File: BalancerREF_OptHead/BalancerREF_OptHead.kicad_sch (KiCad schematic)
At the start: 24 parts, among them J5 TO MAIN BOARD, Q1 AO3400A, U4 TS3021IYLT, U8 TLV9062IDR

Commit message: fix: flip PD1 - the optical comparator could never trip
Confirmed against the netlist, not the description. PD1 was wired cathode to
+3V3 and anode to the transimpedance summing node. The reverse bias is correct
that way, 1.65 V cathode-positive, which is presumably why it survived this long.
The signal direction is not.

Photocurrent leaves the ANODE of a reverse-biased photodiode, so with the anode
on the summing node it was injected into the node rather than pulled out:

  PD1 anode on the node  -> current INTO the summing node
  U8A, U8.2 = IN-        -> inverting TIA, TIA_OUT FALLS
  U8B, gain -120k/10k    -> inverting, OPT_AMP RISES from 1.65 V
  U4, U8.4 = IN-         -> against CMP_THRESHOLD on IN+

CMP_THRESHOLD is 3.3 * 10k/(22k+10k) = 1.016 V with the output low, 1.064 V with
it high - R28's 470k gives 48 mV of hysteresis in the correct direction.
OPT_AMP idles at 1.65 V, AC-coupled to the 1.65 V reference, so it sits 634 mV
ABOVE the threshold and light drove it further away. IN- stayed above IN+ at any
illumination and the output never left its low state. With the Rev F NAND gating
that is total: U9 never falls, U10 never triggers, TR-VERT had no tach at all.

Flipping the diode fixes the chain without touching anything else. Cathode to
PD_TIA_IN, anode to GND: same 1.65 V reverse bias, photocurrent now pulled out of
the node, TIA_OUT rises, OPT_AMP falls through 1.016 V, comparator trips. It
takes about 5.3 uA of photocurrent - 634 mV / 12 / 10k.

Side effect worth having, since Rev F moved Q1 nearer PD1 when it tightened the
emitter loop: the emitter turn-off edge lands inside the synchronous gate window
and cannot be rejected, and after the flip its coupling into the summing node
pushes TIA_OUT the same way darkness does, away from the trip point.

Why none of the existing checks found it. verify_head.py compares the exported
netlist against exact net membership and passed throughout - netlist matched
spec, board matched netlist, ERC clean - because 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
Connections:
- net +3V3: no longer PD1.1 (K)
- net GND: now also PD1.2 (A)
- net PD_TIA_IN: now also PD1.1 (K); no longer PD1.2 (A)

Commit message: feat: optical head rewired in signal-chain order and regrouped for routing
Schematic: components laid out left to right along the signal path and
joined with real wires instead of labelled stubs. One net label per wired
net keeps the PCB's net names. Symbol UUIDs, values and footprints are
untouched. verify_head.py passes and ERC is clean.

Board: pulse loop (C20/R18/Q1/R19/R20) top-left away from PD1's summing
node, TIA and gain stage right of centre, comparator above the connector.
D1 and PD1 stay on the centreline; a BAFFLE rule area (y 116.5 to 124.2,
footprints only) with silk marks reserves the band for the printed
divider. The existing back-side GND pour is unchanged.

Scripts: rewire_head.py and regroup_head.py, both reproducible.

Co-Authored-By: Claude Fable 5.1 <noreply@anthropic.com>
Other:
- note added: "DETECTOR > TRANSIMPEDANCE > x12 AC GAIN"
- note added: "PD1 cathode on the summing node, anode to GND (Rev B): photocurrent is pulled OUT of the node, so TIA_OUT rises, OPT_AMP falls and the comparator can cross 1.016 V. Reversed, U4 never trips."
- note added: "R28 senses U4's own output, upstream of the R32 series damping."
- note added: "SUPPLY + ERC FLAGS"
- note added: "Signal flows left to right: emitter, detector, gain, comparator, cable."
- note removed: "TRANSIMPEDANCE + x12 AC GAIN"
- moved on the sheet: C20, C21, C22, C23, C24, C25, D1, J5, PD1, Q1, R18, R19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

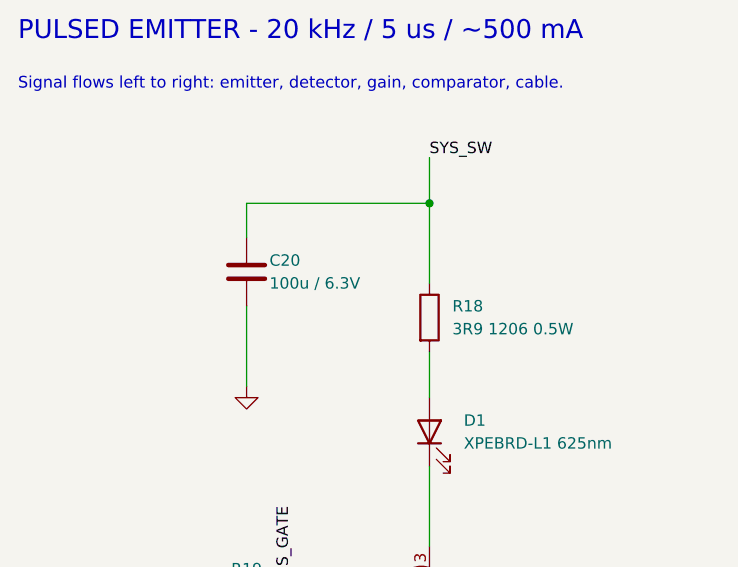
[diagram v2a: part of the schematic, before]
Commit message: fix: BOM fields, silkscreen labels, +3V3 plane, and stale docs before review
- MPN fields: R3/R35/R36 (were "100k"), U9 (was the 1G08), R18 (was 3R0)
- Title block: HOBOVibe spelling; head company line no longer says "human
  review required"
- C20 on the head board rated 10 V; SYS_SW can sit at 5.5 V
- Silkscreen: board name and rev on both boards, battery and MAG polarity,
  pin-1 marks on J4 and both J5
- Main PCB: SYS, SYS_SW, BAT and USB_VBUS tracks removed from In2.Cu so the
  +3V3 plane is whole; three vias that only served them removed. Those four
  nets need re-routing on the outer layers.
- Docs: routing state, ground-pour wording, missing head-board holes,
  JLCPCB parts table rebuilt for the Rev F BOM, superseded LIS2DW12 and
  phototransistor sections marked in DATASHEET-VERIFICATION

Not done here (no KiCad in this environment): re-export of PDF/netlist/ERC/DRC.

Co-Authored-By: Claude Fable 5.1 <noreply@anthropic.com>
Claude-Session: https://claude.ai/code/session_01JeUyuyqf13Zf6V8TjfofPH
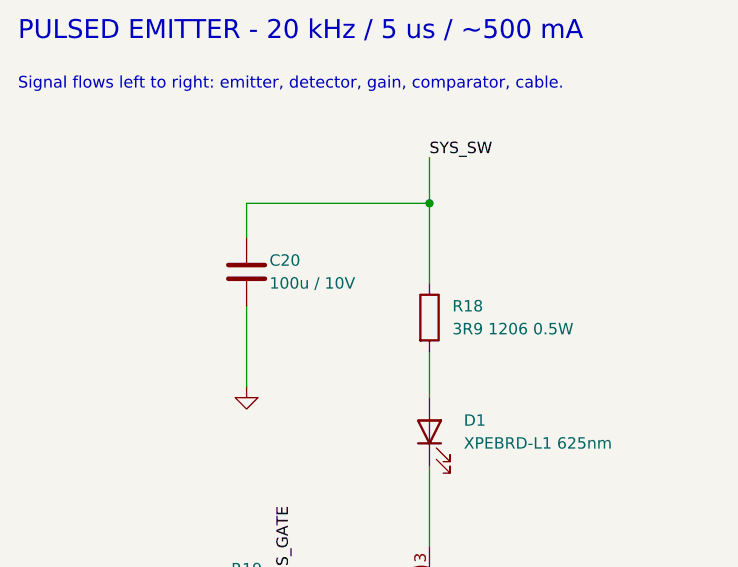
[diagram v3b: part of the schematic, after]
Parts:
- C20: value 100u / 6.3V -> 100u / 10V; MPN 100u / 6.3V -> 100u / 10V
- R18: MPN 3R0 1206 0.5W -> 3R9 1206 0.5W
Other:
- company: Split from BalancerREF Rev C - human review required -> Split from BalancerREF Rev C
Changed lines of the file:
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@@
 		(date "2026-09-11")
 		(rev "B")
-		(company "Split from BalancerREF Rev C - human review required")
+		(company "Split from BalancerREF Rev C")
 		(comment 1 "Cable carries DC rails and digital edges only")
 	)
@@
 			)
 		)
-		(property "Value" "100u / 6.3V"
+		(property "Value" "100u / 10V"
 			(at 58.42 74.93 0)
 			(show_name no)
@@
 			)
 		)
-		(property "MPN" "100u / 6.3V"
+		(property "MPN" "100u / 10V"
 			(at 58.42 72.39 0)
 			(hide yes)
@@
 			)
 		)
-		(property "MPN" "3R0 1206 0.5W"
+		(property "MPN" "3R9 1206 0.5W"
 			(at 78.74 77.47 0)
 			(hide yes)
